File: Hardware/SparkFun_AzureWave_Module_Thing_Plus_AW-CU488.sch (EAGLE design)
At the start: 55 parts, among them J1 THING_PLUS, J3 QWIIC_RA, J5 USB-C, Q1 2.5A/30V, Q2 MBT3904DW1T1, U2 CP210X, U3 AP2112, U4 MCP73831

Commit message: More Layout work - pretty much 99% done
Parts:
- removed LOGO1: SFE_LOGO_FLAME.1_INCH, SparkFun-Aesthetics:SFE_LOGO_FLAME.1_INCH
- removed R16: 12k, SparkFun-Resistors:12KOHM-0603-1/10W-1%
- added LOGO5: SFE_LOGO_NAME_FLAME.1_INCH, SparkFun-Aesthetics:SFE_LOGO_NAME_FLAME.1_INCH
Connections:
- net SCL renamed PA25/SCL
- net SDA renamed PA26/SDA
- removed net N$12: R16.2, U$13.PA28/RREF
- removed net PB3/A6: U$13.PB3/ADC_6
- net GND: no longer R16.1
- net PB5/A1: now also U$13.PB5/ADC_1; no longer U$13.PB5/ADC_1/LP_I2C_SCL
- net PB6/A2: now also U$13.PB6/ADC_2; no longer U$13.PB6/ADC_2/LP_I2C_SDA
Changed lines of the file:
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@@
 <part name="CHG" library="SparkFun-Jumpers" deviceset="JUMPER-SMT_3_1-NC_TRACE" device="_SILK" package3d_urn="urn:adsk.eagle:package:39288/1" value=""/>
 <part name="GND24" library="SparkFun-Aesthetics" deviceset="GND" device=""/>
-<part name="LOGO1" library="SparkFun-Aesthetics" deviceset="SFE_LOGO_FLAME" device=".1_INCH"/>
 <part name="R10" library="SparkFun-Resistors" deviceset="100OHM" device="-0402-TIGHT-1/16W-1%" value="100"/>
 <part name="R14" library="SparkFun-Resistors" deviceset="10KOHM" device="-0402T-1/16W-1%" value="10k"/>
 <part name="R15" library="SparkFun-Resistors" deviceset="1KOHM" device="-0402T-1/16W-1%" value="1k"/>
-<part name="R16" library="SparkFun-Resistors" deviceset="12KOHM" device="-0603-1/10W-1%" value="12k"/>
-<part name="GND23" library="SparkFun-Aesthetics" deviceset="GND" device=""/>
 <part name="C4" library="SparkFun-Capacitors" deviceset="10UF" device="-0603-6.3V-20%" value="10uF"/>
 <part name="GND25" library="SparkFun-Aesthetics" deviceset="GND" device=""/>
@@
 <part name="J2" library="SparkFun-Connectors" deviceset="CONN_03" device="1X03_NO_SILK"/>
 <part name="J6" library="SparkFun-Connectors" deviceset="CONN_02" device="1X02_NO_SILK"/>
+<part name="LOGO5" library="SparkFun-Aesthetics" deviceset="SFE_LOGO_NAME_FLAME" device=".1_INCH"/>
 </parts>
 <sheets>
@@
 <attribute name="VALUE" x="177.8" y="210.82" size="1.778" layer="96" font="vector"/>
 </instance>
-<instance part="LOGO1" gate="G$1" x="40.894" y="18.796" smashed="yes"/>
 <instance part="R10" gate="G$1" x="25.4" y="233.68" smashed="yes">
 <attribute name="NAME" x="25.4" y="235.204" size="1.778" layer="95" font="vector" align="bottom-center"/>
@@
 <attribute name="VALUE" x="237.744" y="22.86" size="1.778" layer="96" font="vector" rot="R90" align="top-center"/>
 </instance>
-<instance part="R16" gate="G$1" x="43.18" y="81.28" smashed="yes">
-<attribute name="NAME" x="43.18" y="82.804" size="1.778" layer="95" font="vector" align="bottom-center"/>
-<attribute name="VALUE" x="43.18" y="79.756" size="1.778" layer="96" font="vector" align="top-center"/>
-</instance>
-<instance part="GND23" gate="1" x="35.56" y="76.2" smashed="yes">
-<attribute name="VALUE" x="33.02" y="73.66" size="1.778" layer="96" font="vector"/>
-</instance>
 <instance part="C4" gate="G$1" x="45.72" y="134.62" smashed="yes">
 <attribute name="NAME" x="47.244" y="137.541" size="1.778" layer="95" font="vector"/>
@@
 <attribute name="NAME" x="172.72" y="40.132" size="1.778" layer="95" font="vector" rot="R180"/>
 </instance>
+<instance part="LOGO5" gate="G$1" x="8.382" y="6.096" smashed="yes"/>
 </instances>
 <busses>
@@
 <pinref part="R15" gate="G$1" pin="1"/>
 <wire x1="236.22" y1="17.78" x2="236.22" y2="15.24" width="0.1524" layer="91"/>
-</segment>
-<segment>
-<pinref part="R16" gate="G$1" pin="1"/>
-<wire x1="38.1" y1="81.28" x2="35.56" y2="81.28" width="0.1524" layer="91"/>
-<wire x1="35.56" y1="81.28" x2="35.56" y2="78.74" width="0.1524" layer="91"/>
-<pinref part="GND23" gate="1" pin="GND"/>
 </segment>
 <segment>
@@
 </segment>
 </net>
-<net name="SDA" class="0">
+<net name="PA26/SDA" class="0">
 <segment>
 <pinref part="J3" gate="G$1" pin="3"/>
@@
 </segment>
 </net>
-<net name="SCL" class="0">
+<net name="PA25/SCL" class="0">
 <segment>
 <pinref part="J3" gate="G$1" pin="4"/>
@@
 </segment>
 </net>
-<net name="N$12" class="0">
-<segment>
-<pinref part="R16" gate="G$1" pin="2"/>
-<wire x1="63.5" y1="81.28" x2="48.26" y2="81.28" width="0.1524" layer="91"/>
-<pinref part="U$13" gate="G$1" pin="PA28/RREF"/>
-</segment>
-</net>
 <net name="PB7/A3" class="0">
 <segment>
@@
 <label x="381" y="147.32" size="1.27" layer="95" font="vector" xref="yes"/>
 <pinref part="J1" gate="G$1" pin="A5"/>
-</segment>
-</net>
-<net name="PB3/A6" class="0">
-<segment>
-<wire x1="124.46" y1="111.76" x2="127" y2="111.76" width="0.1524" layer="91"/>
-<label x="127" y="111.76" size="1.27" layer="95" font="vector" xref="yes"/>
-<pinref part="U$13" gate="G$1" pin="PB3/ADC_6"/>
-</segment>
-<segment>
-<wire x1="416.56" y1="139.7" x2="419.1" y2="139.7" width="0.1524" layer="91"/>
-<label x="419.1" y="139.7" size="1.27" layer="95" font="vector" xref="yes"/>
 </segment>
 </net>
@@
 <wire x1="124.46" y1="106.68" x2="127" y2="106.68" width="0.1524" layer="91"/>
 <label x="127" y="106.68" size="1.27" layer="95" font="vector" xref="yes"/>
-<pinref part="U$13" gate="G$1" pin="PB5/ADC_1/LP_I2C_SCL"/>
+<pinref part="U$13" gate="G$1" pin="PB5/ADC_1"/>
 </segment>
 <segment>
@@
 <wire x1="124.46" y1="104.14" x2="127" y2="104.14" width="0.1524" layer="91"/>
 <label x="127" y="104.14" size="1.27" layer="95" font="vector" xref="yes"/>
-<pinref part="U$13" gate="G$1" pin="PB6/ADC_2/LP_I2C_SDA"/>
-</segment>
-<segment>
+<pinref part="U$13" gate="G$1" pin="PB6/ADC_2"/>
+</segment>
+<segment>

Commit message: pre-design review notes and fixes
-power symbols, Q1, U3, U4 updated to latest libraries
-consolidated all low current signals to 10mils vias. V_USB (x4), 3.3V (x3), VIN (x2)  are still 15mil for higher current capabilities.
-Center anchor for section text in sch
-added via near transitioning digital signals near PB26/PB28 PTH headers
-moved R15 about 20mil to the right to give more room for rework/give more room for the JST connector
-reduced paste on modules pads by 2mils on either side (for a reduction total on the diameter of the paste hole of 4 mils).
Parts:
- Q1: value 2.5A/30V -> 3.1A/30V/105mΩ; device SparkFun-DiscreteSemi:MOSFET-PCHANNELDMG2307L -> SparkFun-DiscreteSemi:MOSFET_PCH-DMG2307L
- R6: device SparkFun-Resistors:2.0KOHM1/10W5%(0603) -> SparkFun-Resistors:2.0KOHM-0603-1/10W-5%
- U3: value AP2112 -> AP2112K-3.3V; device SparkFun-PowerIC:V_REG_LDOSMD -> SparkFun-IC-Power:V_REG_AP2112K-3.3V
- U4: device SparkFun-PowerIC:MCP73831 -> SparkFun-IC-Power:MCP73831
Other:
- note added: "Voltage Regulator"
- note removed: "Voltage Regulator and Battery Charger"

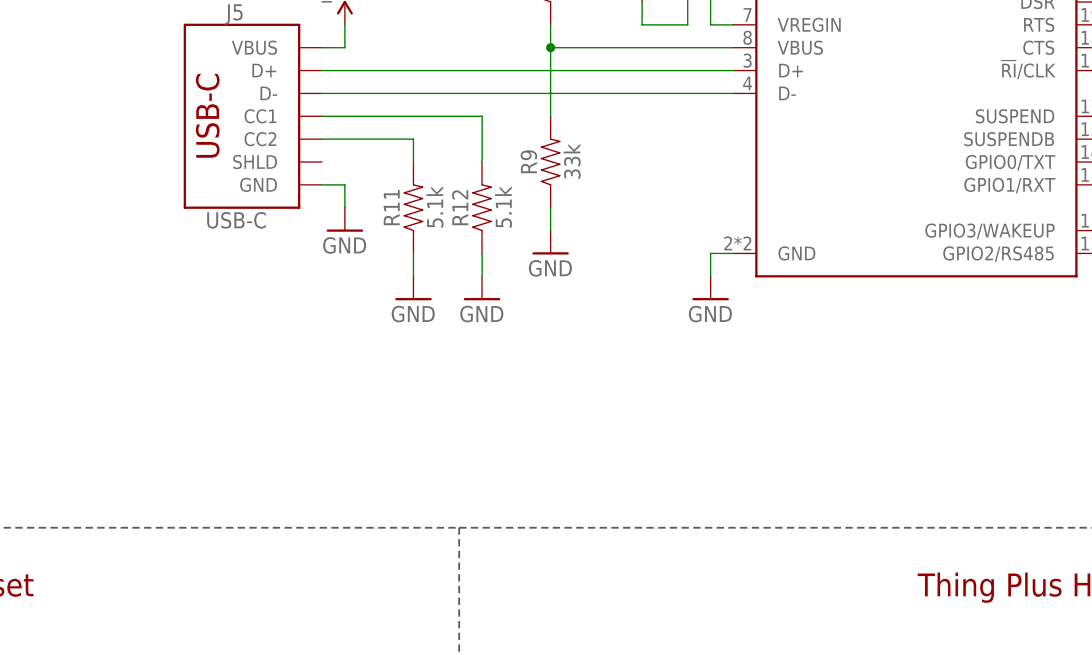
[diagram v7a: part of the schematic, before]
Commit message: added USB Shield GND jumper
-added "shield" net polygons (and via)  to connect all 8 shield pads. And add a little extra strength.
-added jumper to connect USB-C shield to GND (normally closed via trace).
-moved OSHW logo and version text.
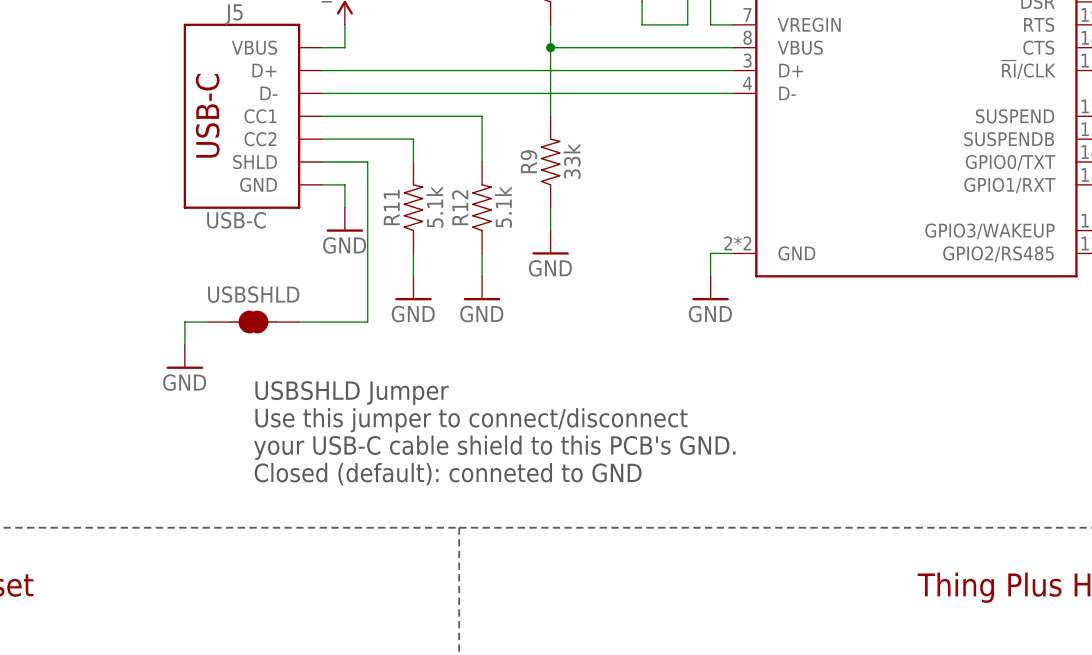
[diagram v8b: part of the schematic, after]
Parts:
- added USBSHLD: JUMPER-SMT_2_NC_TRACE_SILK, SparkFun-Jumpers:JUMPER-SMT_2_NC_TRACE_SILK
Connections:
- new net USB_SHLD: J5.SHLD, USBSHLD.2
- net GND: now also USBSHLD.1
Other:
- note added: "USBSHLD Jumper Use this jumper to connect/disconnect your USB-C cable shield to this PCB's GND. Closed (default): conneted to GND"
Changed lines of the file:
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@@
 <part name="SUPPLY17" library="SparkFun-PowerSymbols" deviceset="VIN" device=""/>
 <part name="SUPPLY7" library="SparkFun-PowerSymbols" deviceset="3.3V" device=""/>
+<part name="USBSHLD" library="SparkFun-Jumpers" deviceset="JUMPER-SMT_2_NC_TRACE" device="_SILK" package3d_urn="urn:adsk.eagle:package:39281/1" value=""/>
+<part name="GND8" library="SparkFun-PowerSymbols" deviceset="GND" device=""/>
 </parts>
 <sheets>
@@
 <wire x1="297.18" y1="106.68" x2="297.18" y2="182.88" width="0.2032" layer="97" style="longdash"/>
 <wire x1="187.96" y1="106.68" x2="187.96" y2="182.88" width="0.2032" layer="97" style="longdash"/>
+<text x="274.32" y="187.96" size="2.032" layer="97" font="vector" rot="MR180" align="top-left">USBSHLD Jumper
+Use this jumper to connect/disconnect
+your USB-C cable shield to this PCB's GND.
+Closed (default): conneted to GND</text>
 </plain>
 <instances>
@@
 <instance part="SUPPLY7" gate="G$1" x="109.22" y="228.6" smashed="yes">
 <attribute name="VALUE" x="109.22" y="231.394" size="1.778" layer="96" font="vector" align="bottom-center"/>
+</instance>
+<instance part="USBSHLD" gate="G$1" x="274.32" y="205.74" smashed="yes">
+<attribute name="NAME" x="274.32" y="208.788" size="1.778" layer="95" font="vector" align="center"/>
+<attribute name="VALUE" x="274.32" y="202.692" size="1.778" layer="96" font="vector" align="center"/>
+</instance>
+<instance part="GND8" gate="1" x="266.7" y="200.66" smashed="yes">
+<attribute name="VALUE" x="264.16" y="198.12" size="1.778" layer="96" font="vector"/>
 </instance>
 </instances>
@@
 <pinref part="GND25" gate="1" pin="GND"/>
 <wire x1="45.72" y1="129.54" x2="45.72" y2="132.08" width="0.1524" layer="91"/>
+</segment>
+<segment>
+<pinref part="USBSHLD" gate="G$1" pin="1"/>
+<wire x1="269.24" y1="205.74" x2="266.7" y2="205.74" width="0.1524" layer="91"/>
+<pinref part="GND8" gate="1" pin="GND"/>
+<wire x1="266.7" y1="205.74" x2="266.7" y2="203.2" width="0.1524" layer="91"/>
 </segment>
 </net>
@@
 </segment>
 </net>
+<net name="USB_SHLD" class="0">
+<segment>
+<pinref part="J5" gate="J1" pin="SHLD"/>
+<wire x1="281.94" y1="223.52" x2="287.02" y2="223.52" width="0.1524" layer="91"/>
+<wire x1="287.02" y1="223.52" x2="287.02" y2="205.74" width="0.1524" layer="91"/>
+<pinref part="USBSHLD" gate="G$1" pin="2"/>
+<wire x1="287.02" y1="205.74" x2="279.4" y2="205.74" width="0.1524" layer="91"/>
+</segment>
+</net>
